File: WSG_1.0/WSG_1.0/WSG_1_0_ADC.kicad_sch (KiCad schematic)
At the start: 50 parts, among them J1 Conn_01x10, U1 ADS131A04IPBSR, U14 TPD4E1U06DBVR, U2 DAC60501ZDGSR, U3 INA827AIDGKR, U4 INA827AIDGKR, U5 INA827AIDGKR, U6 TMP235A2DBZR, Y1 SiT8008AI-13-33S-16.384000

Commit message: new layout started, clusters almost done
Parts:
- removed C11, C27, C4, C5: 0.1uF, Capacitor_SMD:C_0402_1005Metric_Pad0.74x0.62mm_HandSolder, symbol Device:C
- removed C2, C3, C7, C9: 10nF, Capacitor_SMD:C_0402_1005Metric_Pad0.74x0.62mm_HandSolder, symbol Device:C
- added C30: 1nF, Capacitor_SMD:C_0402_1005Metric_Pad0.74x0.62mm_HandSolder, symbol Device:C
- added C39, C40, C41: 2.7nF, Capacitor_SMD:C_0402_1005Metric_Pad0.74x0.62mm_HandSolder, symbol Device:C
- added C42: 680pF, Capacitor_SMD:C_0402_1005Metric_Pad0.74x0.62mm_HandSolder, symbol Device:C
- added R22: 50, Resistor_SMD:R_0402_1005Metric_Pad0.72x0.64mm_HandSolder, symbol Device:R
- added R46, R47, R48, R49, R50, R51, R52, R53: 100, Resistor_SMD:R_0402_1005Metric_Pad0.72x0.64mm_HandSolder, symbol Device:R
- R18: now not fitted
- U1: footprint Package_QFP:TQFP-32_7x7mm_P0.8mm -> Package_QFP:TQFP-32_5x5mm_P0.5mm
- U3, U4, U5: footprint Package_SO:VSSOP-8_2.3x2mm_P0.5mm -> Package_SO:VSSOP-8_3x3mm_P0.65mm
- Y1: value SiT8008AI-13-33S-16.384000 -> SiT8008AI-12-33S-16.384000
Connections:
- net AIN0P: now also C39.1, R46.2; no longer U3.7 (VOUT)
- net AIN1P: now also C40.1, R47.2; no longer U4.7 (VOUT)
- net AIN2P: now also C41.1, R48.2; no longer U5.7 (VOUT)
- net AIN3P: now also C42.1, R49.2; no longer U6.2 (VOUT)
- net CLK16M: now also R22.1; no longer Y1.3 (OUT)
- net GND: now also C30.1, C39.2, C40.2, C41.2, C42.2
- net VREF_1V65: now also C30.2, R50.1, R51.1, R52.1, R53.1; no longer U1.1 (AIN1N), U1.3 (AIN2N), U1.5 (AIN3N), U1.7 (AIN4N)
- new net: R46.1, U3.7 (VOUT)
- new net: R53.2, U1.7 (AIN4N)
- new net: R49.1, U6.2 (VOUT)
- new net: R48.1, U5.7 (VOUT)
- new net: R51.2, U1.1 (AIN1N)
- new net: R50.2, U1.3 (AIN2N)
- new net: R52.2, U1.5 (AIN3N)
- new net: R22.2, Y1.3 (OUT)
- new net: R47.1, U4.7 (VOUT)
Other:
- moved on the sheet: C22, C23, C24, C25, C35, R1, R15, R19, R2, R28, R3, U1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

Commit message: new layout, trying different layout onw
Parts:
- added C31: 1uF, Capacitor_SMD:C_0402_1005Metric_Pad0.74x0.62mm_HandSolder, symbol Device:C
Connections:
- net 3V3A: now also C31.2
- net GND: now also C31.1
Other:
- moved on the sheet: C28
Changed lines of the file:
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@@
 	)
 	(junction
-		(at 113.03 170.18)
+		(at 212.09 27.94)
 		(diameter 0)
 		(color 0 0 0 0)
 	)
 	(junction
-		(at 121.92 104.14)
+		(at 113.03 170.18)
 		(diameter 0)
 		(color 0 0 0 0)
 	)
 	(junction
-		(at 262.89 30.48)
+		(at 121.92 104.14)
 		(diameter 0)
 		(color 0 0 0 0)
 	)
 	(junction
-		(at 212.09 30.48)
+		(at 262.89 30.48)
 		(diameter 0)
 		(color 0 0 0 0)
@@
 	(wire
 		(pts
-			(xy 212.09 30.48) (xy 212.09 36.83)
-		)
-		(stroke
-			(width 0)
-			(type default)
-		)
-	)
-	(wire
-		(pts
 			(xy 179.07 125.73) (xy 187.96 125.73)
 		)
@@
 	(wire
 		(pts
+			(xy 212.09 27.94) (xy 212.09 36.83)
+		)
+		(stroke
+			(width 0)
+			(type default)
+		)
+	)
+	(wire
+		(pts
 			(xy 231.14 111.76) (xy 231.14 113.03)
 		)
@@
 	(wire
 		(pts
-			(xy 207.01 30.48) (xy 212.09 30.48)
+			(xy 207.01 27.94) (xy 212.09 27.94)
 		)
 		(stroke
@@
 	(global_label "3V3A"
 		(shape input)
-		(at 207.01 30.48 180)
+		(at 207.01 27.94 180)
 		(fields_autoplaced yes)
 		(effects
@@
 		)
 		(property "Intersheetrefs" "${INTERSHEET_REFS}"
-			(at 199.4286 30.48 0)
+			(at 199.4286 27.94 0)
 			(hide yes)
 			(show_name no)
@@
 	(symbol
 		(lib_id "Device:C")
-		(at 212.09 26.67 0)
+		(at 212.09 24.13 0)
 		(unit 1)
 		(body_style 1)
@@
 		(dnp no)
 		(property "Reference" "C28"
-			(at 209.042 25.654 0)
+			(at 209.042 23.114 0)
 			(show_name no)
 			(do_not_autoplace no)
@@
 		)
 		(property "Value" "0.1uF"
-			(at 209.042 23.114 0)
+			(at 209.042 20.574 0)
 			(show_name no)
 			(do_not_autoplace no)
@@
 		)
 		(property "Footprint" "Capacitor_SMD:C_0402_1005Metric_Pad0.74x0.62mm_HandSolder"
-			(at 213.0552 30.48 0)
+			(at 213.0552 27.94 0)
 			(hide yes)
 			(show_name no)
@@
 		)
 		(property "Datasheet" ""
-			(at 212.09 26.67 0)
+			(at 212.09 24.13 0)
 			(hide yes)
 			(show_name no)
@@
 		)
 		(property "Description" "Unpolarized capacitor"
-			(at 212.09 26.67 0)
+			(at 212.09 24.13 0)
 			(hide yes)
 			(show_name no)
@@
 	(symbol
 		(lib_id "power:GND")
-		(at 212.09 22.86 180)
+		(at 212.09 20.32 180)
 		(unit 1)
 		(body_style 1)
@@
 		(fields_autoplaced yes)
 		(property "Reference" "#PWR061"
-			(at 212.09 16.51 0)
+			(at 212.09 13.97 0)
 			(hide yes)
 			(show_name no)
@@
 		)
 		(property "Value" "GND"
-			(at 212.09 17.78 0)
+			(at 212.09 15.24 0)
 			(show_name no)
 			(do_not_autoplace no)
@@
 		)
 		(property "Footprint" ""
-			(at 212.09 22.86 0)
+			(at 212.09 20.32 0)
 			(hide yes)
 			(show_name no)
@@
 		)
 		(property "Datasheet" ""
-			(at 212.09 22.86 0)
+			(at 212.09 20.32 0)
 			(hide yes)
 			(show_name no)
@@
 		)
 		(property "Description" "Power symbol creates a global label with name \"GND\" , ground"
-			(at 212.09 22.86 0)
+			(at 212.09 20.32 0)
 			(hide yes)
 			(show_name no)
@@
 	(symbol
 		(lib_id "power:GND")
+		(at 219.71 27.94 90)
+		(unit 1)
+		(body_style 1)
+		(exclude_from_sim no)
+		(in_bom yes)
+		(on_board yes)
+		(in_pos_files yes)
+		(dnp no)
+		(property "Reference" "#PWR065"
+			(at 226.06 27.94 0)
+			(hide yes)
+			(show_name no)
+			(do_not_autoplace no)
+			(effects
+				(font
+					(size 1.27 1.27)
+				)
+			)
+		)
+		(property "Value" "GND"
+			(at 222.758 26.162 90)
+			(show_name no)
+			(do_not_autoplace no)
+			(effects
+				(font
+					(size 1.27 1.27)
+				)
+			)
+		)
+		(property "Footprint" ""
+			(at 219.71 27.94 0)
+			(hide yes)
+			(show_name no)
+			(do_not_autoplace no)
+			(effects
+				(font
+					(size 1.27 1.27)
+				)
+			)
+		)
+		(property "Datasheet" ""
+			(at 219.71 27.94 0)
+			(hide yes)
+			(show_name no)
+			(do_not_autoplace no)
+			(effects
+				(font
+					(size 1.27 1.27)
+				)
+			)
+		)
+		(property "Description" "Power symbol creates a global label with name \"GND\" , ground"
+			(at 219.71 27.94 0)
+			(hide yes)
+			(show_name no)
+			(do_not_autoplace no)
+			(effects
+				(font
+					(size 1.27 1.27)
+				)
+			)
+		)
+		(pin "1"
+		)
+		(instances
+			(project "WSG_1.0"
+				(path "/cb65811d-b245-4002-a5a3-eef29f2c4ddb/c5ed03a7-f581-4366-93a5-60fa505a706c"
+					(reference "#PWR065")
+					(unit 1)
+				)
+			)
+		)
+	)
+	(symbol
+		(lib_id "power:GND")
 		(at 182.88 68.58 180)
 		(unit 1)
@@
 					(unit 1)
 				)
+			)
+		)
+	)
+	(symbol
+		(lib_id "Device:C")
+		(at 215.9 27.94 270)
+		(unit 1)
+		(body_style 1)
+		(exclude_from_sim no)
+		(in_bom yes)
+		(on_board yes)
+		(in_pos_files yes)
+		(dnp no)
+		(property "Reference" "C31"
+			(at 218.44 33.782 90)
+			(show_name no)
+			(do_not_autoplace no)
+			(effects
+				(font
+					(size 1.27 1.27)
+				)
+				(justify right)
+			)
+		)
+		(property "Value" "1uF"
+			(at 218.44 31.242 90)
+			(show_name no)
+			(do_not_autoplace no)
+			(effects
+				(font
+					(size 1.27 1.27)
+				)
+				(justify right)
+			)
+		)
+		(property "Footprint" "Capacitor_SMD:C_0402_1005Metric_Pad0.74x0.62mm_HandSolder"
+			(at 212.09 28.9052 0)
+			(hide yes)
+			(show_name no)
+			(do_not_autoplace no)
+			(effects
+				(font
+					(size 1.27 1.27)
+				)
+			)
+		)
+		(property "Datasheet" ""
+			(at 215.9 27.94 0)
+			(hide yes)
+			(show_name no)
+			(do_not_autoplace no)
+			(effects
+				(font
+					(size 1.27 1.27)
+				)
+			)
+		)
+		(property "Description" "Unpolarized capacitor"
+			(at 215.9 27.94 0)
+			(hide yes)
+			(show_name no)
+			(do_not_autoplace no)
+			(effects
+				(font
+					(size 1.27 1.27)
+				)
+			)
+		)
+		(pin "1"
+		)
+		(pin "2"
+		)
+		(instances
+			(project "WSG_1.0"
+				(path "/cb65811d-b245-4002-a5a3-eef29f2c4ddb/c5ed03a7-f581-4366-93a5-60fa505a706c"
+					(reference "C31")
+					(unit 1)
+				)

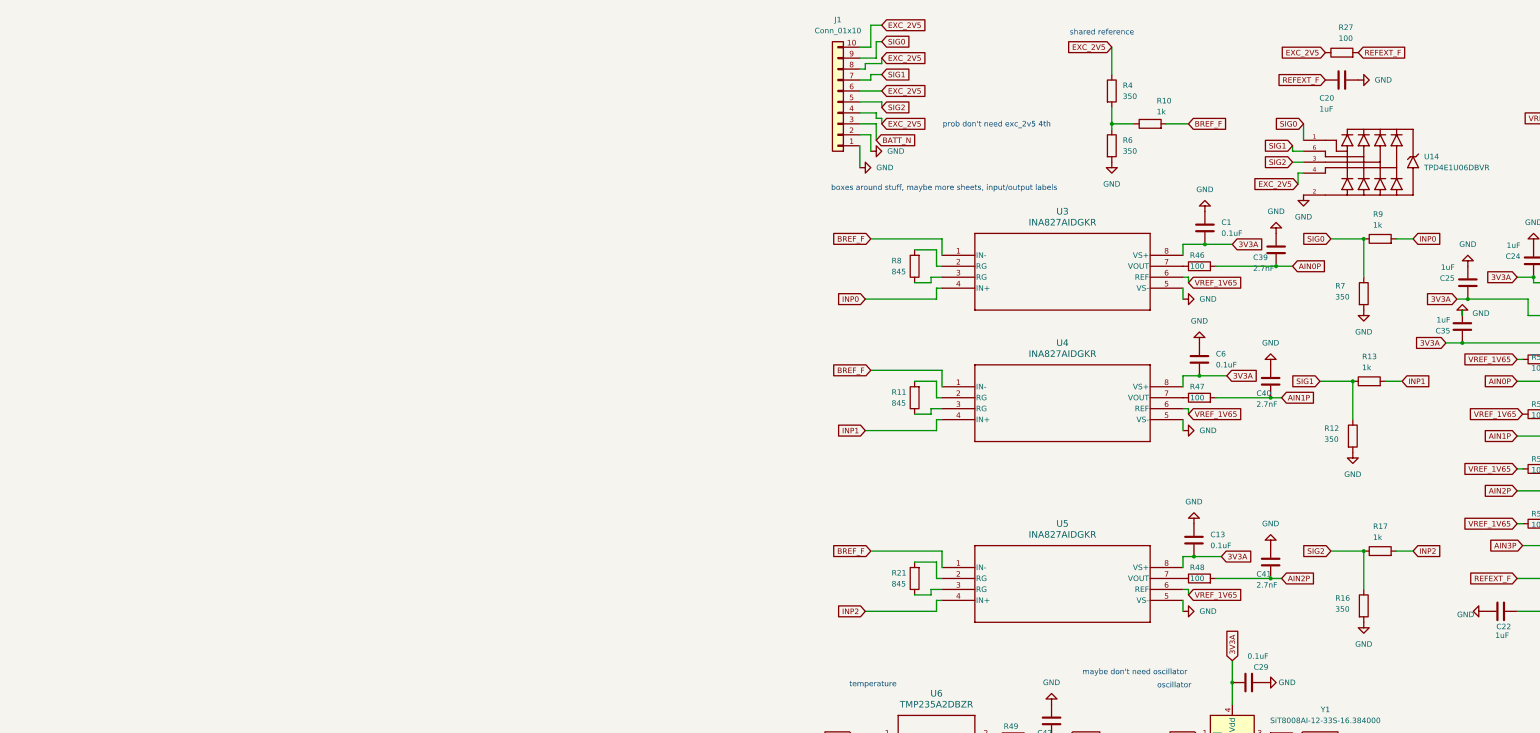
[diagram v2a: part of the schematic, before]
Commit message: adc schematic reforming
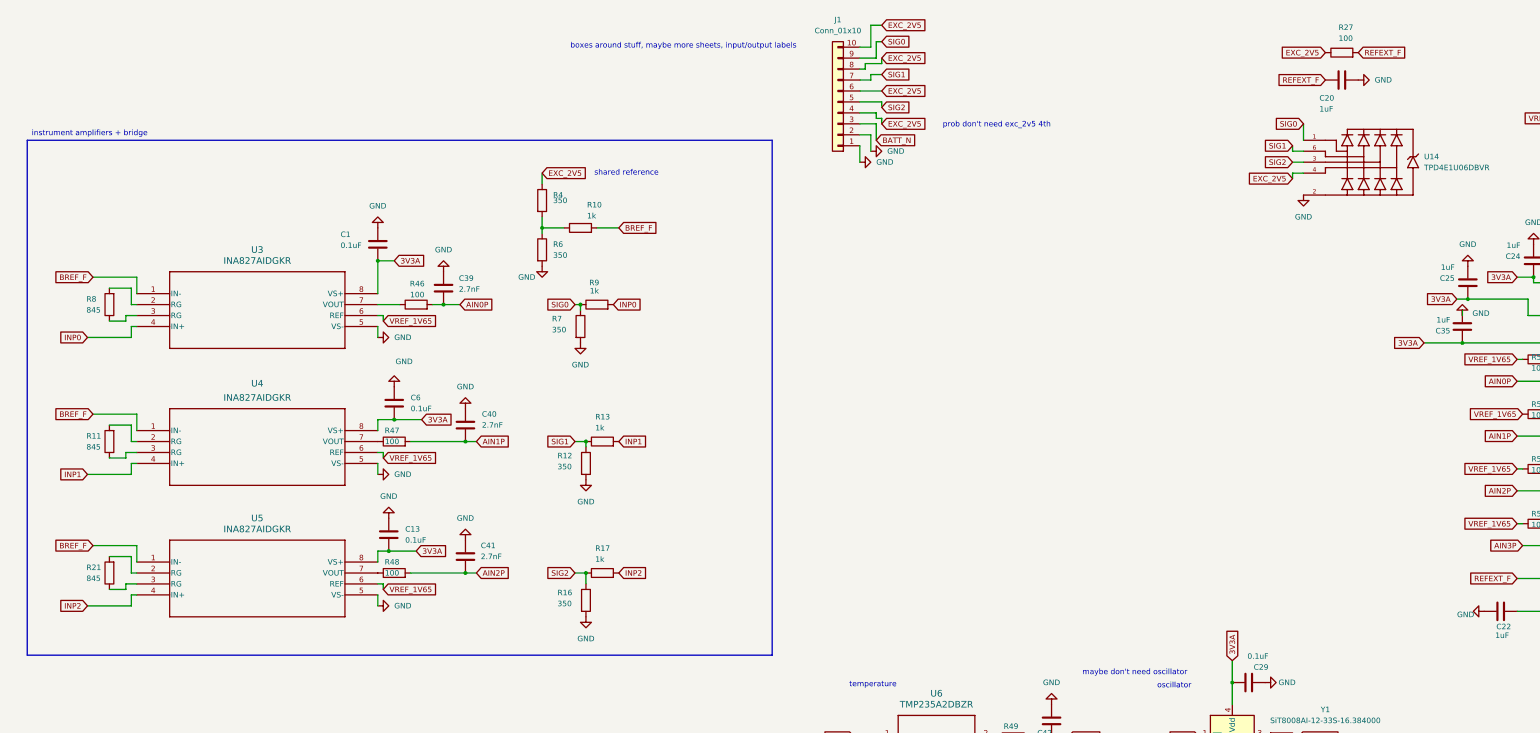
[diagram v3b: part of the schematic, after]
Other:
- note added: "instrument amplifiers + bridge"
- moved on the sheet: C1, C13, C39, C40, C41, C6, R10, R11, R12, R13, R16, R17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

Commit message: ~1/2 done with routing, neeed to undo some
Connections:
- net REFEXT_F: no longer C20.1, R27.2
- new net: C20.1, R27.2
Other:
- note added: "ADC/DAC"
- note added: "MEMS Oscillator"
- note added: "TVS"
- note added: "Temperature Sensor"
- note added: "VNCPEN = 0"
- note added: "WSG Connector"
- note removed: "boxes around stuff, maybe more sheets, input/output labels"
- note removed: "maybe don't need oscillator"
- note removed: "oscillator"
- note removed: "prob not need neg charge pump VNCPEN = 0"
- note removed: "temperature"
- moved on the sheet: C1, C13, C20, C21, C22, C23, C24, C25, C26, C28, C29, C30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

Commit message: organized schematic, new layouT
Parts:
- C26: value 150nF -> 220nF
- C39, C40, C41, C42: Dielectric (none) -> C0G/NP0
- J1: footprint Connector_PinHeader_2.00mm:PinHeader_2x05_P2.00mm_Horizontal -> Connector_PinHeader_2.00mm:PinHeader_2x05_P2.00mm_Vertical
- Y1: value SiT8008AI-12-33S-16.384000 -> SiT8008AI-13-33S-16.384000
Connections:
- net REFEXT_F: now also C20.1, R27.2
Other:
- note added: "G = 5 + 80k/845 = 99.67, ~100 REF pins = 1.65 V mid-supply"
- note added: "REFEXT filter 100R+1uF"
- note added: "Ratiometric: EXC_2V5 = excitation = ADC reference -> excitation noise/drift cancels to 1st order. Sensitivity 1.281 mV per 1000 ue at INA input; full scale +/-11,750 ue; chain noise ~0.24 ue rms. can't find INA specs at 3.3V"
- note added: "ST pin tied high (always on) DigiKey programmed-to-order"
- note added: "all ADC/DAC uses 3V3A"
- moved on the sheet: C20, R27
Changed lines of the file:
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@@
 	(rectangle
 		(start 12.7 15.24)
-		(end 48.26 66.04)
+		(end 48.26 53.34)
 		(stroke
 			(width 0)
@@
 	(text "prob don't need exc_2v5 4th"
 		(exclude_from_sim no)
-		(at 27.178 68.834 0)
+		(at 26.162 55.88 0)
+		(effects
+			(font
+				(size 1.27 1.27)
+			)
+		)
+	)
+	(text "Ratiometric: EXC_2V5 = excitation = ADC reference -> excitation noise/drift cancels to 1st order.\nSensitivity 1.281 mV per 1000 ue at INA input; full scale +/-11,750 ue; chain noise ~0.24 ue rms.\ncan't find INA specs at 3.3V "
+		(exclude_from_sim no)
+		(at 62.738 5.08 0)
 		(effects
 			(font
@@
 	(text "shared reference"
 		(exclude_from_sim no)
-		(at 152.908 88.9 0)
+		(at 137.414 85.852 0)
 		(effects
 			(font
@@
 		)
 	)
+	(text "all ADC/DAC uses 3V3A"
+		(exclude_from_sim no)
+		(at 197.104 16.51 0)
+		(effects
+			(font
+				(size 1.27 1.27)
+			)
+		)
+	)
+	(text "REFEXT filter 100R+1uF"
+		(exclude_from_sim no)
+		(at 272.542 165.1 0)
+		(effects
+			(font
+				(size 1.27 1.27)
+			)
+		)
+	)
+	(text "G = 5 + 80k/845 = 99.67, ~100\nREF pins = 1.65 V mid-supply"
+		(exclude_from_sim no)
+		(at 32.766 102.616 0)
+		(effects
+			(font
+				(size 1.27 1.27)
+			)
+		)
+	)
 	(text "MEMS Oscillator"
 		(exclude_from_sim no)
@@
 		)
 	)
+	(text "ST pin tied high (always on)\nDigiKey programmed-to-order"
+		(exclude_from_sim no)
+		(at 136.398 14.224 0)
+		(effects
+			(font
+				(size 1.27 1.27)
+			)
+		)
+	)
 	(junction
 		(at 187.96 48.26)
@@
 	(wire
 		(pts
+			(xy 271.78 158.75) (xy 270.51 158.75)
+		)
+		(stroke
+			(width 0)
+			(type default)
+		)
+	)
+	(wire
+		(pts
 			(xy 95.25 186.69) (xy 95.25 189.23)
 		)
@@
 		)
 	)
+	(global_label "REFEXT_F"
+		(shape input)
+		(at 271.78 158.75 90)
+		(fields_autoplaced yes)
+		(effects
+			(font
+				(size 1.27 1.27)
+			)
+			(justify left)
+		)
+		(property "Intersheetrefs" "${INTERSHEET_REFS}"
+			(at 271.78 146.8749 90)
+			(hide yes)
+			(show_name no)
+			(do_not_autoplace no)
+			(effects
+				(font
+					(size 1.27 1.27)
+				)
+				(justify left)
+			)
+		)
+	)
 	(global_label "ADC_MISO"
 		(shape input)
@@
 	(global_label "EXC_2V5"
 		(shape input)
-		(at 24.13 59.69 180)
+		(at 262.89 158.75 180)
 		(fields_autoplaced yes)
 		(effects
@@
 		)
 		(property "Intersheetrefs" "${INTERSHEET_REFS}"
-			(at 13.0411 59.69 0)
+			(at 251.8011 158.75 0)
 			(hide yes)
 			(show_name no)
@@
 		)
 		(property "Value" "350"
-			(at 135.89 95.2499 0)
+			(at 135.89 95.758 0)
 			(show_name no)
 			(do_not_autoplace no)
@@
 			)
 		)
-		(property "Value" "150nF"
+		(property "Value" "220nF"
 			(at 247.142 28.194 0)
 			(show_name no)
@@
 			)
 		)
+		(property "Dielectric" "C0G/NP0"
+			(at 110.49 115.57 0)
+			(hide yes)
+			(show_name no)
+			(do_not_autoplace no)
+			(effects
+				(font
+					(size 1.27 1.27)
+				)
+			)
+		)
 		(pin "1"
 		)
@@
 			)
 		)
-		(property "Value" "SiT8008AI-12-33S-16.384000"
+		(property "Value" "SiT8008AI-13-33S-16.384000"
 			(at 140.208 43.688 0)
 			(show_name no)
@@
 			)
 		)
+		(property "Dielectric" "C0G/NP0"
+			(at 115.57 147.32 0)
+			(hide yes)
+			(show_name no)
+			(do_not_autoplace no)
+			(effects
+				(font
+					(size 1.27 1.27)
+				)
+			)
+		)
 		(pin "1"
 		)
@@
 	(symbol
 		(lib_id "power:GND")
-		(at 39.37 59.69 90)
+		(at 279.4 158.75 90)
 		(unit 1)
 		(body_style 1)
@@
 		(fields_autoplaced yes)
 		(property "Reference" "#PWR053"
-			(at 45.72 59.69 0)
+			(at 285.75 158.75 0)
 			(hide yes)
 			(show_name no)
@@
 		)
 		(property "Value" "GND"
-			(at 43.18 59.6899 90)
+			(at 283.21 158.7499 90)
 			(show_name no)
 			(do_not_autoplace no)
@@
 		)
 		(property "Footprint" ""
-			(at 39.37 59.69 0)
+			(at 279.4 158.75 0)
 			(hide yes)
 			(show_name no)
@@
 		)
 		(property "Datasheet" ""
-			(at 39.37 59.69 0)
+			(at 279.4 158.75 0)
 			(hide yes)
 			(show_name no)
@@
 		)
 		(property "Description" "Power symbol creates a global label with name \"GND\" , ground"
-			(at 39.37 59.69 0)
+			(at 279.4 158.75 0)
 			(hide yes)
 			(show_name no)
@@
 	(symbol
 		(lib_id "Device:C")
-		(at 35.56 59.69 90)
+		(at 275.59 158.75 90)
 		(unit 1)
 		(body_style 1)
@@
 		(dnp no)
 		(property "Reference" "C20"
-			(at 30.353 63.881 90)
+			(at 277.368 154.178 90)
 			(show_name no)
 			(do_not_autoplace no)
@@
 		)
 		(property "Value" "1uF"
-			(at 30.353 66.421 90)
+			(at 277.368 156.718 90)
 			(show_name no)
 			(do_not_autoplace no)
@@
 		)
 		(property "Footprint" "Capacitor_SMD:C_0402_1005Metric_Pad0.74x0.62mm_HandSolder"
-			(at 39.37 58.7248 0)
+			(at 279.4 157.7848 0)
 			(hide yes)
 			(show_name no)
@@
 		)
 		(property "Datasheet" ""
-			(at 35.56 59.69 0)
+			(at 275.59 158.75 0)
 			(hide yes)
 			(show_name no)
@@
 		)
 		(property "Description" "Unpolarized capacitor"
-			(at 35.56 59.69 0)
+			(at 275.59 158.75 0)
 			(hide yes)
 			(show_name no)
@@
 			)
 		)
+		(property "Dielectric" "C0G/NP0"
+			(at 115.57 177.8 0)
+			(hide yes)
+			(show_name no)
+			(do_not_autoplace no)
+			(effects
+				(font
+					(size 1.27 1.27)
+				)
+			)
+		)
 		(pin "1"
 		)
@@
 			)
 		)
+		(property "Dielectric" "C0G/NP0"
+			(at 106.68 59.69 0)
+			(hide yes)
+			(show_name no)
+			(do_not_autoplace no)
+			(effects
+				(font
+					(size 1.27 1.27)
+				)
+			)
+		)
 		(pin "1"
 		)
@@
 			)
 		)
-		(property "Footprint" "Connector_PinHeader_2.00mm:PinHeader_2x05_P2.00mm_Horizontal"
+		(property "Footprint" "Connector_PinHeader_2.00mm:PinHeader_2x05_P2.00mm_Vertical"
 			(at 20.32 36.83 0)
 			(hide yes)
@@
 	(symbol
 		(lib_id "Device:R")
-		(at 27.94 59.69 90)
+		(at 266.7 158.75 90)
 		(unit 1)
 		(body_style 1)
@@
 		(dnp no)
 		(property "Reference" "R27"
-			(at 27.178 53.848 90)
+			(at 263.144 154.178 90)
 			(show_name no)
 			(do_not_autoplace no)
@@
 		)
 		(property "Value" "100"
-			(at 27.178 56.388 90)
+			(at 263.144 156.718 90)
 			(show_name no)
 			(do_not_autoplace no)
@@
 		)
 		(property "Footprint" "Resistor_SMD:R_0402_1005Metric_Pad0.72x0.64mm_HandSolder"
-			(at 27.94 61.468 90)
+			(at 266.7 160.528 90)
 			(hide yes)
 			(show_name no)
@@
 		)
 		(property "Datasheet" ""
-			(at 27.94 59.69 0)
+			(at 266.7 158.75 0)
 			(hide yes)
 			(show_name no)
@@
 		)
 		(property "Description" "Resistor"
-			(at 27.94 59.69 0)
+			(at 266.7 158.75 0)
 			(hide yes)
 			(show_name no)
